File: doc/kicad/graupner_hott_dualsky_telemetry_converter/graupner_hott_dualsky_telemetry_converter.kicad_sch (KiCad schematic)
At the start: 4 parts, among them J1 Graupner HoTT Telemetry Port, J2 Dualsky/KISS Telemetry In

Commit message: updated docs
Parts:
- A1: value Arduino_Leonardo -> Arduino Pro Micro (ATMega32u)
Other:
- title: (none) -> Dualsky ESC Summit (KISS) telemetry to HoTT converter
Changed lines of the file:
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@@
 	(generator_version "9.0")
 	(paper "A5")
+	(title_block
+		(title "Dualsky ESC Summit (KISS) telemetry to HoTT converter")
+	)
 	(junction
 		(at 85.09 68.58)
@@
 		(on_board yes)
 		(dnp no)
-		(fields_autoplaced yes)
 		(property "Reference" "A1"
 			(at 113.9033 30.48 0)
@@
 			)
 		)
-		(property "Value" "Arduino_Leonardo"
-			(at 113.9033 33.02 0)
-			(effects
-				(font
+		(property "Value" "Arduino Pro Micro (ATMega32u)"
+			(at 104.902 28.194 0)
+			(effects
+				(font

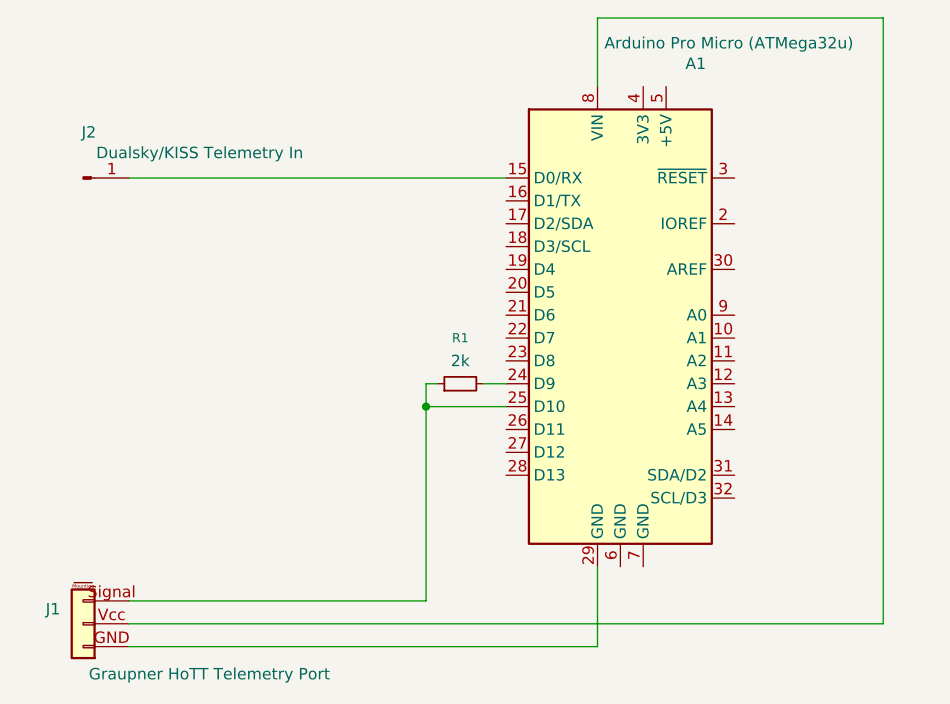
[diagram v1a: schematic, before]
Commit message: fixed HoTT resistor according to HoTTServer.h
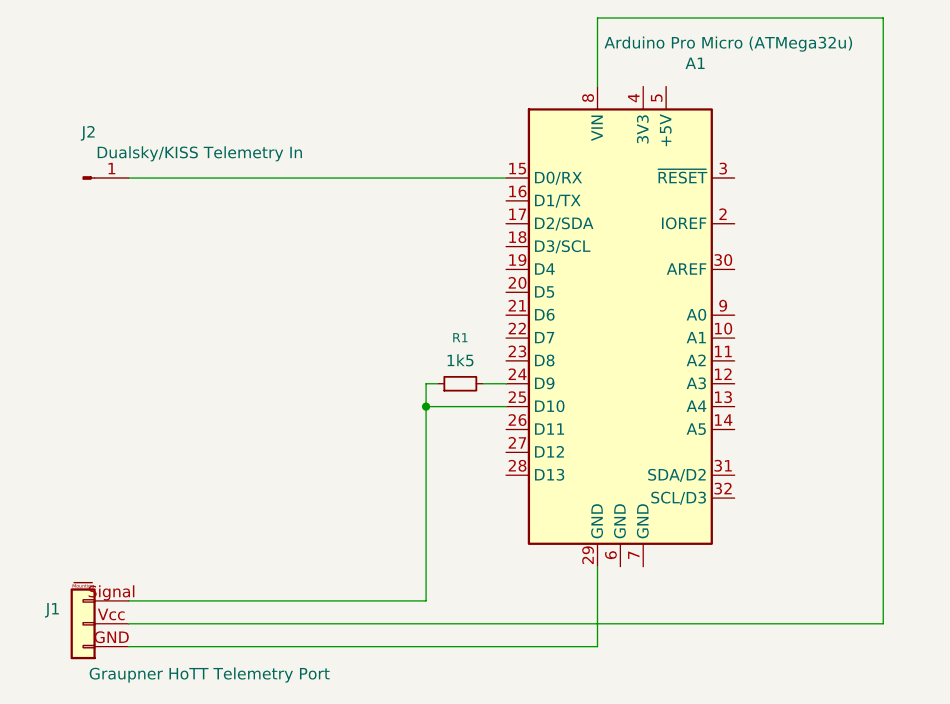
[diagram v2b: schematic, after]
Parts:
- R1: value 2k -> 1k5
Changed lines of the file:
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@@
 			)
 		)
-		(property "Value" "2k"
+		(property "Value" "1k5"
 			(at 88.9 63.5 90)
 			(effects
